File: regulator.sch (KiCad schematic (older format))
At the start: 6 parts, among them U2 LD1117V33

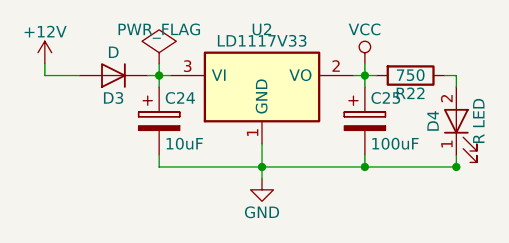
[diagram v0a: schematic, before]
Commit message: Reduce the line driver back to simple
After determining the gain needed to be 0.735 (which is out of spec for
the amp), I was unsure what to do with the 2nd order filter on the amp.
It wasn't even present on the headphone amp from before, and I suspect
the head unit in the car does some filtering of its own. To simplify
things, I removed the second order filter and went back to a simple line
driver. I also set the values of the gain setting resistors to 8.2 and
11, which gets as close as I can to 0.735 gain using single E24
resistors.
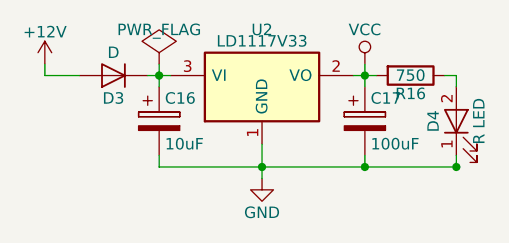
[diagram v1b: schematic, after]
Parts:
- renumbered C24 to C16, C25 to C17, R22 to R16
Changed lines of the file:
@@
 $EndDescr
 $Comp
-L GND #PWR041
+L GND #PWR039
 U 1 1 59484363
 P 5500 4500
-F 0 "#PWR041" H 5500 4250 50  0001 C CNN
+F 0 "#PWR039" H 5500 4250 50  0001 C CNN
 F 1 "GND" H 5500 4350 50  0000 C CNN
 F 2 "" H 5500 4500 50  0001 C CNN
@@
 	5500 4350 5500 4500
 $Comp
-L +12V #PWR042
+L +12V #PWR040
 U 1 1 59484575
 P 4550 4000
-F 0 "#PWR042" H 4550 3850 50  0001 C CNN
+F 0 "#PWR040" H 4550 3850 50  0001 C CNN
 F 1 "+12V" H 4550 4140 50  0000 C CNN
 F 2 "" H 4550 4000 50  0001 C CNN
@@
 	5950 4000 5950 4100
 $Comp
-L CP C24
+L CP C16
 U 1 1 59484D99
 P 5050 4250
-F 0 "C24" H 5075 4350 50  0000 L CNN
+F 0 "C16" H 5075 4350 50  0000 L CNN
 F 1 "10uF" H 5075 4150 50  0000 L CNN
 F 2 "blubaru:CP_Radial_D4.0mm_P1.50mm" H 5088 4100 50  0001 C CNN
@@
 $EndComp
 $Comp
-L CP C25
+L CP C17
 U 1 1 59484E96
 P 5950 4250
-F 0 "C25" H 5975 4350 50  0000 L CNN
+F 0 "C17" H 5975 4350 50  0000 L CNN
 F 1 "100uF" H 5975 4150 50  0000 L CNN
 F 2 "blubaru:CP_Radial_D6.3mm_P2.50mm" H 5988 4100 50  0001 C CNN
@@
 Connection ~ 5950 4050
 $Comp
-L VCC #PWR043
+L VCC #PWR041
 U 1 1 59486886
 P 5950 4000
-F 0 "#PWR043" H 5950 3850 50  0001 C CNN
+F 0 "#PWR041" H 5950 3850 50  0001 C CNN
 F 1 "VCC" H 5950 4150 50  0000 C CNN
 F 2 "" H 5950 4000 50  0001 C CNN
@@
 	5900 4050 6000 4050
 $Comp
-L R R22
+L R R16
 U 1 1 594DE951
 P 6150 4050
-F 0 "R22" V 6230 4050 50  0000 C CNN
+F 0 "R16" V 6230 4050 50  0000 C CNN
 F 1 "750" V 6150 4050 50  0000 C CNN
 F 2 "Resistors_THT:R_Axial_DIN0204_L3.6mm_D1.6mm_P5.08mm_Horizontal" V 6080 4050 50  0001 C CNN
@@
 	5000 4050 5100 4050
 $Comp
-L PWR_FLAG #FLG044
+L PWR_FLAG #FLG042
 U 1 1 597583E7
 P 5050 4000
-F 0 "#FLG044" H 5050 4075 50  0001 C CNN
+F 0 "#FLG042" H 5050 4075 50  0001 C CNN
 F 1 "PWR_FLAG" H 5050 4150 50  0000 C CNN
 F 2 "" H 5050 4000 50  0001 C CNN
